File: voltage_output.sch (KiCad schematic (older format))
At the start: 20 parts, among them P2 CONN_01X01, P3 CONN_01X01, Q1 Q_NPN_BEC, SW3 SW_SPDT, SW4 SW_Rotary12

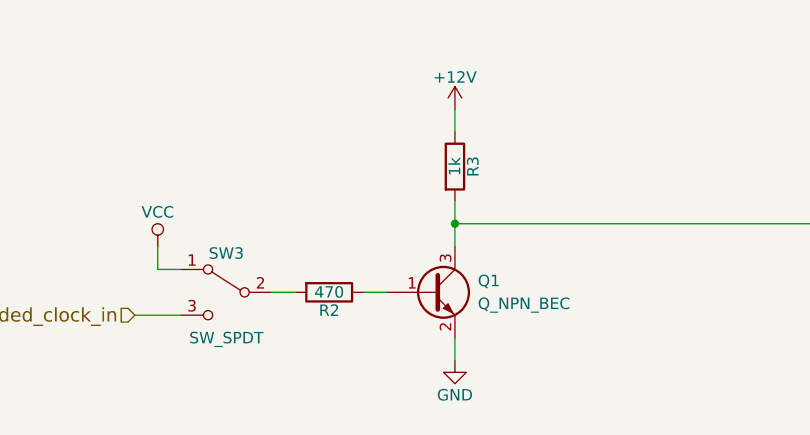
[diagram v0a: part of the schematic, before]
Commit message: Added testpoints for VCC, 12V, and GND
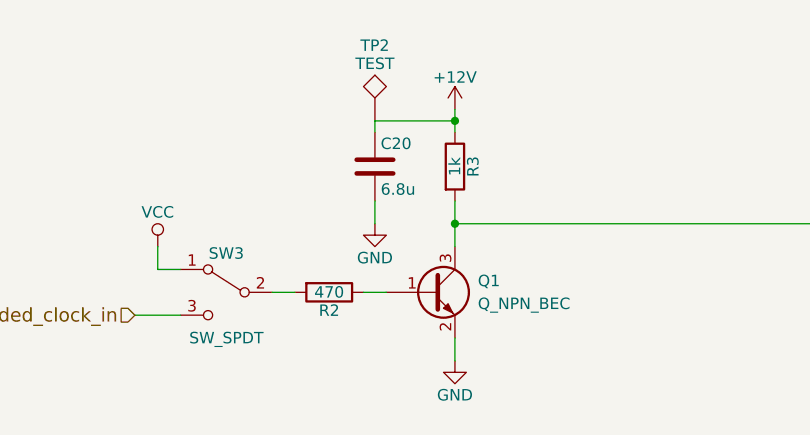
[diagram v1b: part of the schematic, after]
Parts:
- added C20: 6.8u, Capacitors_SMD:C_0805_HandSoldering, symbol C
- added TP2: TEST, Measurement_Points:Measurement_Point_Square-TH_Big, symbol TEST
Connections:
- net +12V: now also C20.1, TP2.1
- net GND: now also C20.2
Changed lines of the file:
@@
 Wire Wire Line
 	1300 2100 1500 2100
+$Comp
+L C C20
+U 1 1 58C9DD95
+P 2350 1450
+F 0 "C20" H 2375 1550 50  0000 L CNN
+F 1 "6.8u" H 2375 1350 50  0000 L CNN
+F 2 "Capacitors_SMD:C_0805_HandSoldering" H 2388 1300 50  0001 C CNN
+F 3 "" H 2350 1450 50  0000 C CNN
+	1    2350 1450
+	1    0    0    -1
+$EndComp
+$Comp
+L GND #PWR068
+U 1 1 58C9DDF5
+P 2350 1700
+F 0 "#PWR068" H 2350 1450 50  0001 C CNN
+F 1 "GND" H 2350 1550 50  0000 C CNN
+F 2 "" H 2350 1700 50  0000 C CNN
+F 3 "" H 2350 1700 50  0000 C CNN
+	1    2350 1700
+	1    0    0    -1
+$EndComp
+Wire Wire Line
+	2350 1700 2350 1600
+Wire Wire Line
+	2350 1300 2350 1250
+Wire Wire Line
+	2350 1250 2700 1250
+Connection ~ 2700 1250
+$Comp
+L TEST TP2
+U 1 1 58C9E47A
+P 2350 1250
+F 0 "TP2" H 2350 1550 50  0000 C BNN
+F 1 "TEST" H 2350 1500 50  0000 C CNN
+F 2 "Measurement_Points:Measurement_Point_Square-TH_Big" H 2350 1250 50  0001 C CNN
+F 3 "" H 2350 1250 50  0000 C CNN
+	1    2350 1250
+	1    0    0    -1
+$EndComp
 $EndSCHEMATC

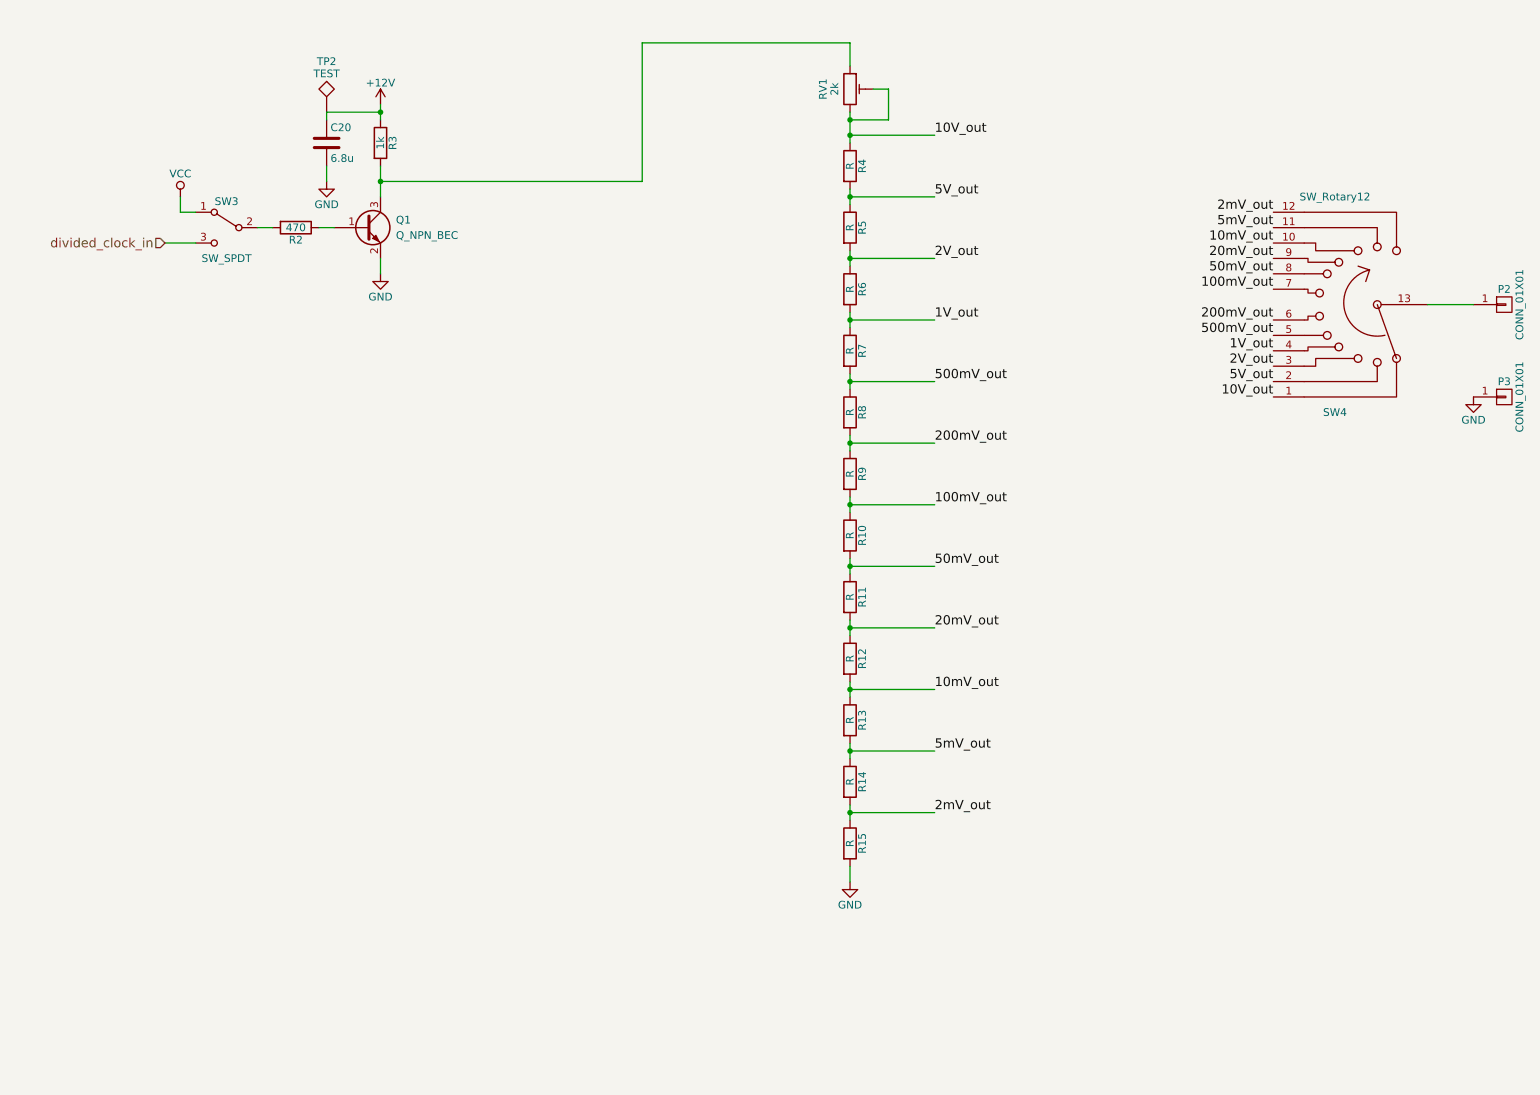
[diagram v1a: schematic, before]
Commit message: Updated voltage output divider to use practical resistor values
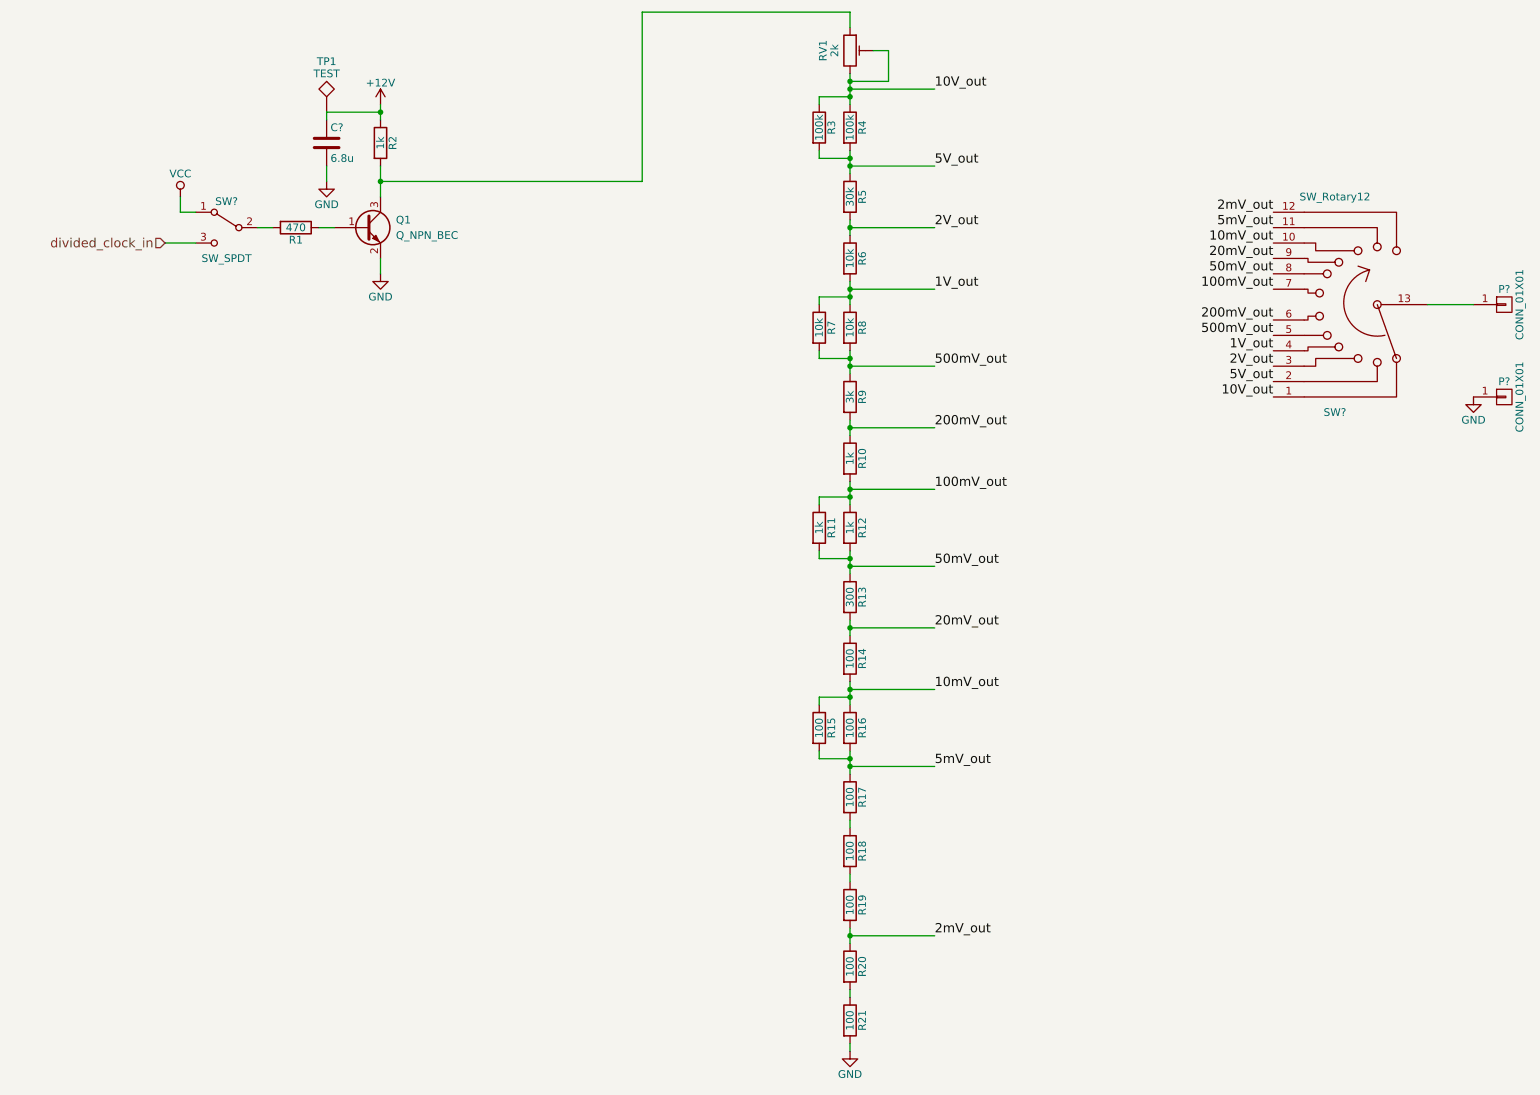
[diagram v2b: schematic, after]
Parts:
- added R11: 1k, Resistors_SMD:R_0805_HandSoldering, symbol R
- added R15, R18, R19, R20: 100, Resistors_SMD:R_0805_HandSoldering, symbol R
- added R3: 100k, Resistors_SMD:R_0805_HandSoldering, symbol R
- added R7: 10k, Resistors_SMD:R_0805_HandSoldering, symbol R
- R10: renamed from R9; value R -> 1k
- R12: renamed from R10; value R -> 1k
- R13: renamed from R11; value R -> 300
- R14: renamed from R12; value R -> 100
- R16: renamed from R13; value R -> 100
- R17: renamed from R14; value R -> 100
- R21: renamed from R15; value R -> 100
- R4: value R -> 100k
- R5: value R -> 30k
- R6: value R -> 10k
- R8: renamed from R7; value R -> 10k
- R9: renamed from R8; value R -> 3k
- renumbered C20 to C?, P2 to P?, P3 to P?, R2 to R1, R3 to R2, SW3 to SW?, SW4 to SW?, TP2 to TP1
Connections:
- net 100mV_out: now also R11.1
- net 10V_out: now also R3.1
- net 10mV_out: now also R15.1
- net 1V_out: now also R7.1
- net 2mV_out: now also R19.2, R20.1; no longer R17.2, R21.1
- net 500mV_out: now also R7.2
- net 50mV_out: now also R11.2
- net 5V_out: now also R3.2
- net 5mV_out: now also R15.2
- new net: R17.2, R18.1
- new net: R20.2, R21.1
- new net: R18.2, R19.1
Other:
- moved on the sheet: R10, R12, R16, R17, R21, R4, R5, R6, R8, R9, RV1
